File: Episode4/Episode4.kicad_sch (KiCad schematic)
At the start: 38 parts, among them J1 CARD, J10 CARD, J11 CARD, J12 CARD, J13 CARD, J14 CARD, J2 CARD, J3 CARD, J4 CARD, J5 CARD, J6 CARD, J7 ATX POWER, J8 BB Con, J9 CARD, SW1 POWER, U1 74HCT14, U2 74HCT74

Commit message: Finished the backplane
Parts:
- added C169, C186: 0.1µF, Capacitor_SMD:C_0805_2012Metric_Pad1.18x1.45mm_HandSolder, symbol Device:C_Small
- added D6: +5V, LED_SMD:LED_1206_3216Metric_Pad1.42x1.75mm_HandSolder, symbol Device:LED_Filled
- added D7: +3V3, LED_SMD:LED_1206_3216Metric_Pad1.42x1.75mm_HandSolder, symbol Device:LED_Filled
- added D8: +12V, LED_SMD:LED_1206_3216Metric_Pad1.42x1.75mm_HandSolder, symbol Device:LED_Filled
- added D9: -12V, LED_SMD:LED_1206_3216Metric_Pad1.42x1.75mm_HandSolder, symbol Device:LED_Filled
- added R1: 1K5, Resistor_SMD:R_0805_2012Metric_Pad1.20x1.40mm_HandSolder, symbol Device:R_US
- added R2: 620, Resistor_SMD:R_0805_2012Metric_Pad1.20x1.40mm_HandSolder, symbol Device:R_US
- added R3, R4: 4K7, Resistor_SMD:R_0805_2012Metric_Pad1.20x1.40mm_HandSolder, symbol Device:R_US
- C185: renamed from C2; symbol Device:C -> Device:C_Small; Manufacturer_Name Samsung Electro-Mechanics -> TAIYO YUDEN; Manufacturer_Part_Number CL21B105KBFNNNG -> MCASU21GSB7105KTNA01
- C191: renamed from C1; symbol Device:C -> Device:C_Small; Manufacturer_Name Samsung Electro-Mechanics -> TAIYO YUDEN; Manufacturer_Part_Number CL21B105KBFNNNG -> MCASU21GSB7105KTNA01
- H1, H10, H4: now fitted; now left out of the parts list
- H2: renamed from H3; now fitted; now left out of the parts list
- H3: renamed from H7; now fitted; now left out of the parts list
- H5: renamed from H6; now fitted; now left out of the parts list
- H6: renamed from H9; now fitted; now left out of the parts list
- H7: renamed from H2; now fitted; now left out of the parts list
- H8: renamed from H5; now fitted; now left out of the parts list
- H9: renamed from H8; now fitted; now left out of the parts list
- J1: renamed from J8; value BB Con -> BREAK-OUT; Manufacturer_Name 3M Electronic Solutions Division -> Preci-dip; Manufacturer_Part_Number 929852-01-36-RA -> 803-87-036-10-005101
- J10: renamed from J11; value CARD -> SLOT
- J11: renamed from J12; value CARD -> SLOT
- J12: renamed from J13; value CARD -> SLOT
- J13: renamed from J14; value CARD -> SLOT
- J14: renamed from J7; symbol 0_Library:ATX_PSU_CONN -> MicroHobbyist:ATX_PSU_CONN
- J2: renamed from J1; value CARD -> SLOT
- J3: renamed from J2; value CARD -> SLOT
- J4: renamed from J3; value CARD -> SLOT
- J5: renamed from J4; value CARD -> SLOT
- J6: renamed from J5; value CARD -> SLOT
- J7: renamed from J6; value CARD -> SLOT
- J8: renamed from J9; value CARD -> SLOT
- J9: renamed from J10; value CARD -> SLOT
- U1: renamed from U2; Function (none) -> DIV2
- U2: renamed from U1; Function (none) -> OSC
- renumbered D5 to D1, D1 to D2, D2 to D4, D4 to D5, R1 to R5, R4 to R6, R2 to R7, R3 to R8
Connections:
- net +12V: now also R3.1
- net +3V3: now also R2.1; no longer J14.1 (+3.3V), J14.13 (+3.3V)
- net +5V: now also R1.1
- net -12V: now also R4.1
- net GND: now also C169.2, C186.2, D6.1 (K), D7.1 (K), D8.1 (K), D9.2 (A)
- net VCC: now also C169.1, C186.1
- net FIRQ1 renamed ~{FIRQ1}
- net FIRQ2 renamed ~{FIRQ2}
- net FIRQ3 renamed ~{FIRQ3}
- new net: D8.2 (A), R3.2
- new net: D6.2 (A), R1.2
- new net: D7.2 (A), R2.2
- new net: D9.1 (K), R4.2
- no-connect marks 9 -> 11
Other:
- note added: "ATX Power Connector"
- note added: "ATX Power ON Circuit"
- note added: "Bypass Capacitors"
- note added: "Power Indicators"
- note removed: "ATX POWER CONNECTOR"
- note removed: "ATX POWER ON CIRCUIT"
- moved on the sheet: C185, C191, D1, D2, D3, D4, D5, J1, J10, J11, J12, J13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

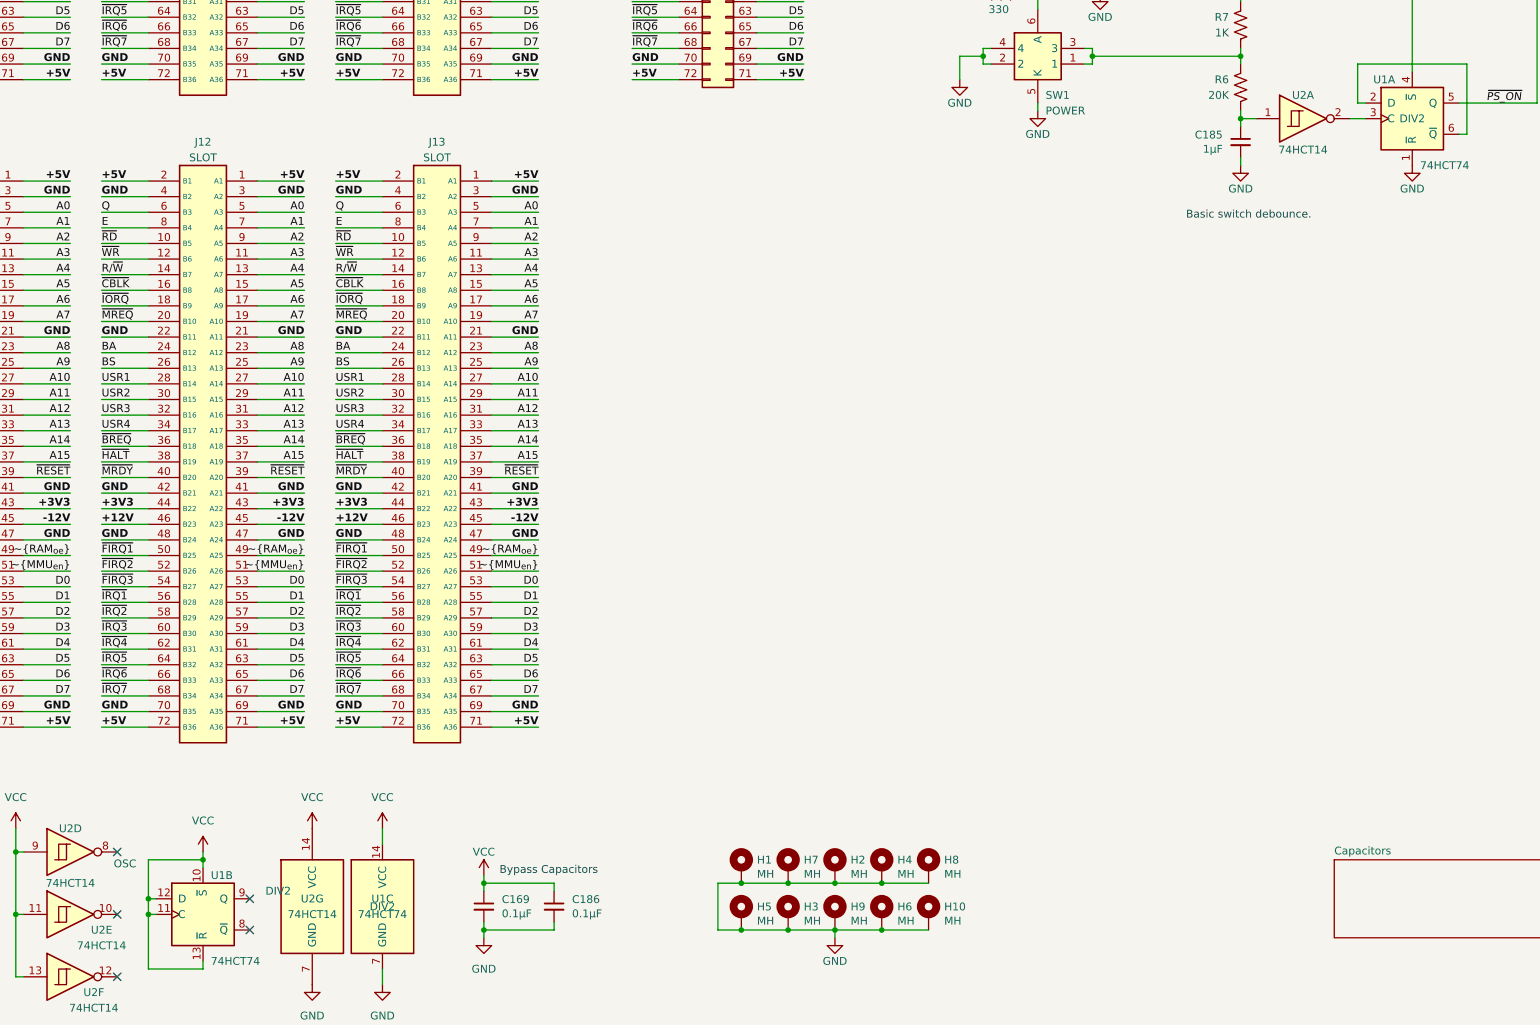
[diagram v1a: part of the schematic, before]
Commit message: Moved power traces from inner CU to back CU
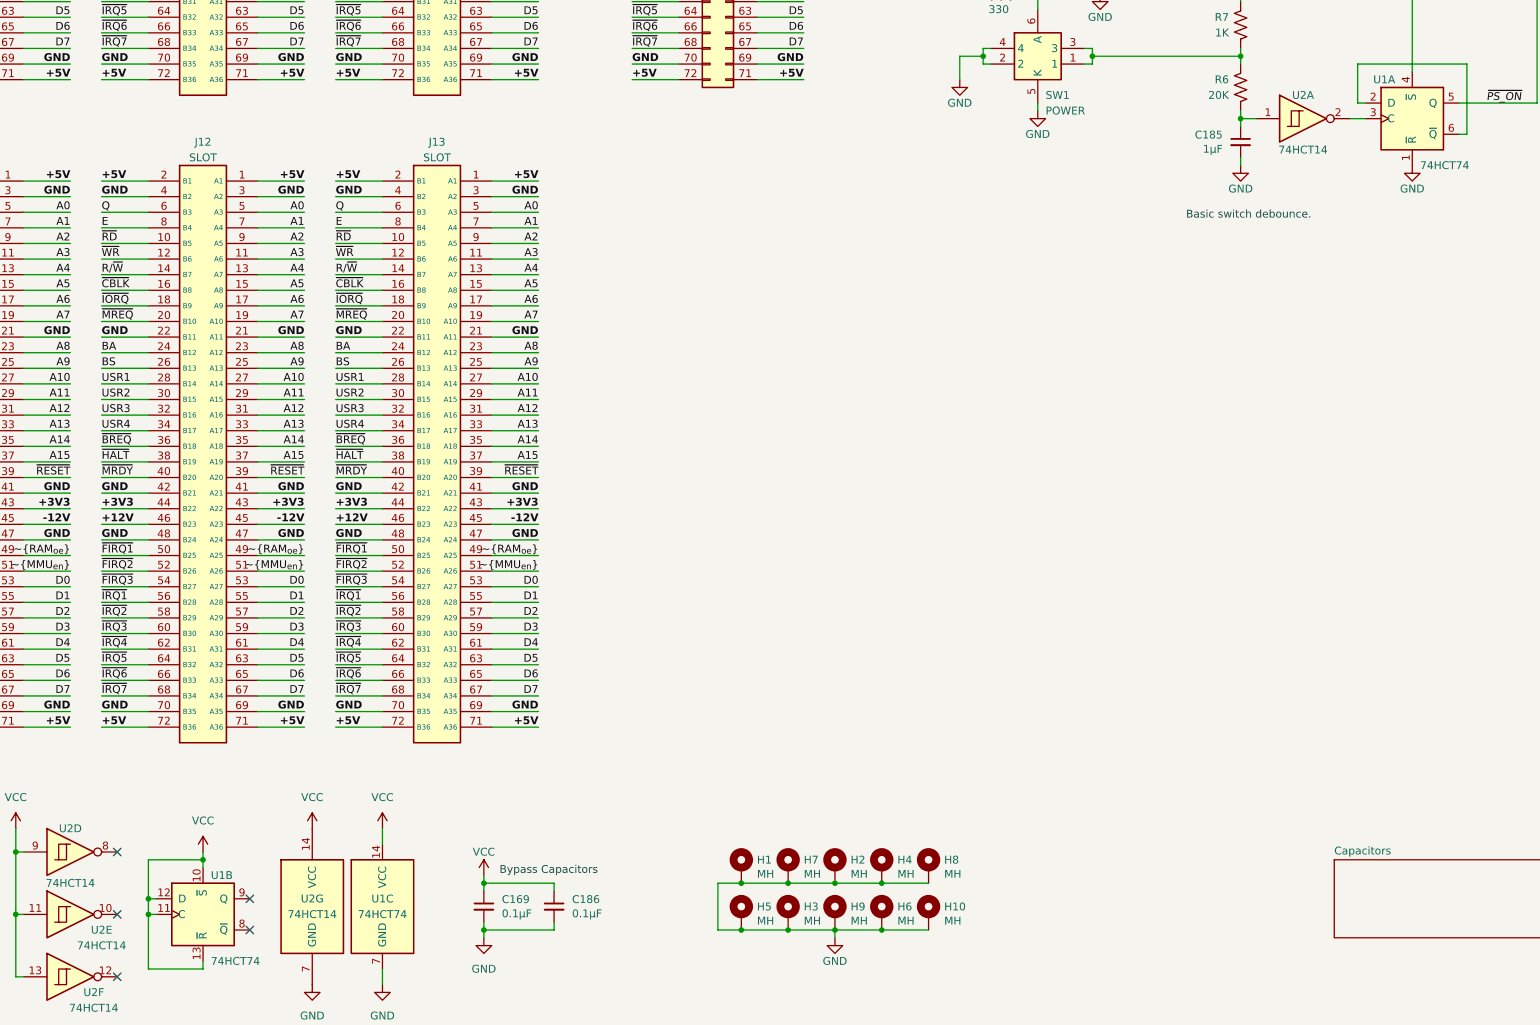
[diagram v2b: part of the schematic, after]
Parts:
- U1: Function DIV2 -> (none)
- U2: Function OSC -> (none)
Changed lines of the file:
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@@
 			)
 		)
-		(property "Function" "OSC"
-			(at 369.57 86.36 0)
-			(effects
-				(font
-					(size 1.27 1.27)
-				)
-				(hide yes)
-			)
-		)
-		(property "Function_2" ""
-			(at 369.57 86.36 0)
-			(effects
-				(font
-					(size 1.27 1.27)
-				)
-				(hide yes)
-			)
-		)
 		(property "Sim.Device" ""
 			(at 369.57 86.36 0)
@@
 			)
 		)
-		(property "Function" "OSC"
-			(at 203.2 243.84 0)
-			(effects
-				(font
-					(size 1.27 1.27)
-				)
-				(hide yes)
-			)
-		)
-		(property "Function_2" ""
-			(at 203.2 243.84 0)
-			(effects
-				(font
-					(size 1.27 1.27)
-				)
-				(hide yes)
-			)
-		)
 		(property "Sim.Device" ""
 			(at 203.2 243.84 0)
@@
 			)
 		)
-		(property "Function" "OSC"
-			(at 364.49 115.57 0)
-			(effects
-				(font
-					(size 1.27 1.27)
-				)
-				(hide yes)
-			)
-		)
-		(property "Function_2" ""
-			(at 364.49 115.57 0)
-			(effects
-				(font
-					(size 1.27 1.27)
-				)
-				(hide yes)
-			)
-		)
 		(property "Sim.Device" ""
 			(at 364.49 115.57 0)
@@
 			)
 		)
-		(property "Function" "OSC"
-			(at 163.83 255.27 0)
-			(effects
-				(font
-					(size 1.27 1.27)
-				)
-				(hide yes)
-			)
-		)
-		(property "Function_2" ""
-			(at 163.83 255.27 0)
-			(effects
-				(font
-					(size 1.27 1.27)
-				)
-				(hide yes)
-			)
-		)
 		(property "Sim.Device" ""
 			(at 163.83 255.27 0)
@@
 			)
 		)
-		(property "Function" "OSC"
-			(at 172.72 236.855 0)
-			(effects
-				(font
-					(size 1.27 1.27)
-				)
-			)
-		)
-		(property "Function_2" ""
-			(at 163.83 234.95 0)
-			(effects
-				(font
-					(size 1.27 1.27)
-				)
-				(hide yes)
-			)
-		)
 		(property "Sim.Device" ""
 			(at 163.83 234.95 0)
@@
 			)
 		)
-		(property "Function" "DIV2"
-			(at 195.58 241.3 0)
-			(effects
-				(font
-					(size 1.27 1.27)
-				)
-				(justify left)
-			)
-		)
-		(property "Function_2" ""
-			(at 185.42 245.11 0)
-			(effects
-				(font
-					(size 1.27 1.27)
-				)
-				(hide yes)
-			)
-		)
 		(property "Sim.Device" ""
 			(at 185.42 245.11 0)
@@
 			)
 		)
-		(property "Function" "DIV2"
-			(at 382.27 115.57 0)
-			(effects
-				(font
-					(size 1.27 1.27)
-				)
-			)
-		)
-		(property "Function_2" ""
-			(at 382.27 115.57 0)
-			(effects
-				(font
-					(size 1.27 1.27)
-				)
-				(hide yes)
-			)
-		)
 		(property "Sim.Device" ""
 			(at 382.27 115.57 0)
@@
 			)
 		)
-		(property "Function" "DIV2"
-			(at 214.63 243.84 0)
-			(effects
-				(font
-					(size 1.27 1.27)
-				)
-			)
-		)
-		(property "Function_2" ""
-			(at 214.63 243.84 0)
-			(effects
-				(font
-					(size 1.27 1.27)
-				)
-				(hide yes)
-			)
-		)
 		(property "Sim.Device" ""
 			(at 214.63 243.84 0)
@@
 			)
 		)
-		(property "Function" "OSC"
-			(at 341.63 86.36 0)
-			(effects
-				(font
-					(size 1.27 1.27)
-				)
-				(hide yes)
-			)
-		)
-		(property "Function_2" ""
-			(at 341.63 86.36 0)
-			(effects
-				(font
-					(size 1.27 1.27)
-				)
-				(hide yes)
-			)
-		)
 		(property "Sim.Device" ""
 			(at 341.63 86.36 0)
@@
 			(at 163.83 245.11 0)
 			(effects
-				(font
-					(size 1.27 1.27)
-				)
-				(hide yes)
-			)
-		)
-		(property "Function" "OSC"
-			(at 163.83 245.11 0)
-			(effects
-				(font
-					(size 1.27 1.27)
-				)
-				(hide yes)
-			)
-		)
-		(property "Function_2" ""
-			(at 163.83 245.11 0)
-			(effects
